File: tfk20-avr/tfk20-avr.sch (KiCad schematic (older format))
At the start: 25 parts, among them J101 USB_C_Receptacle_USB2.0, SW101 SW_Push, U101 ATmega32U4-AU, Y101 16MHz

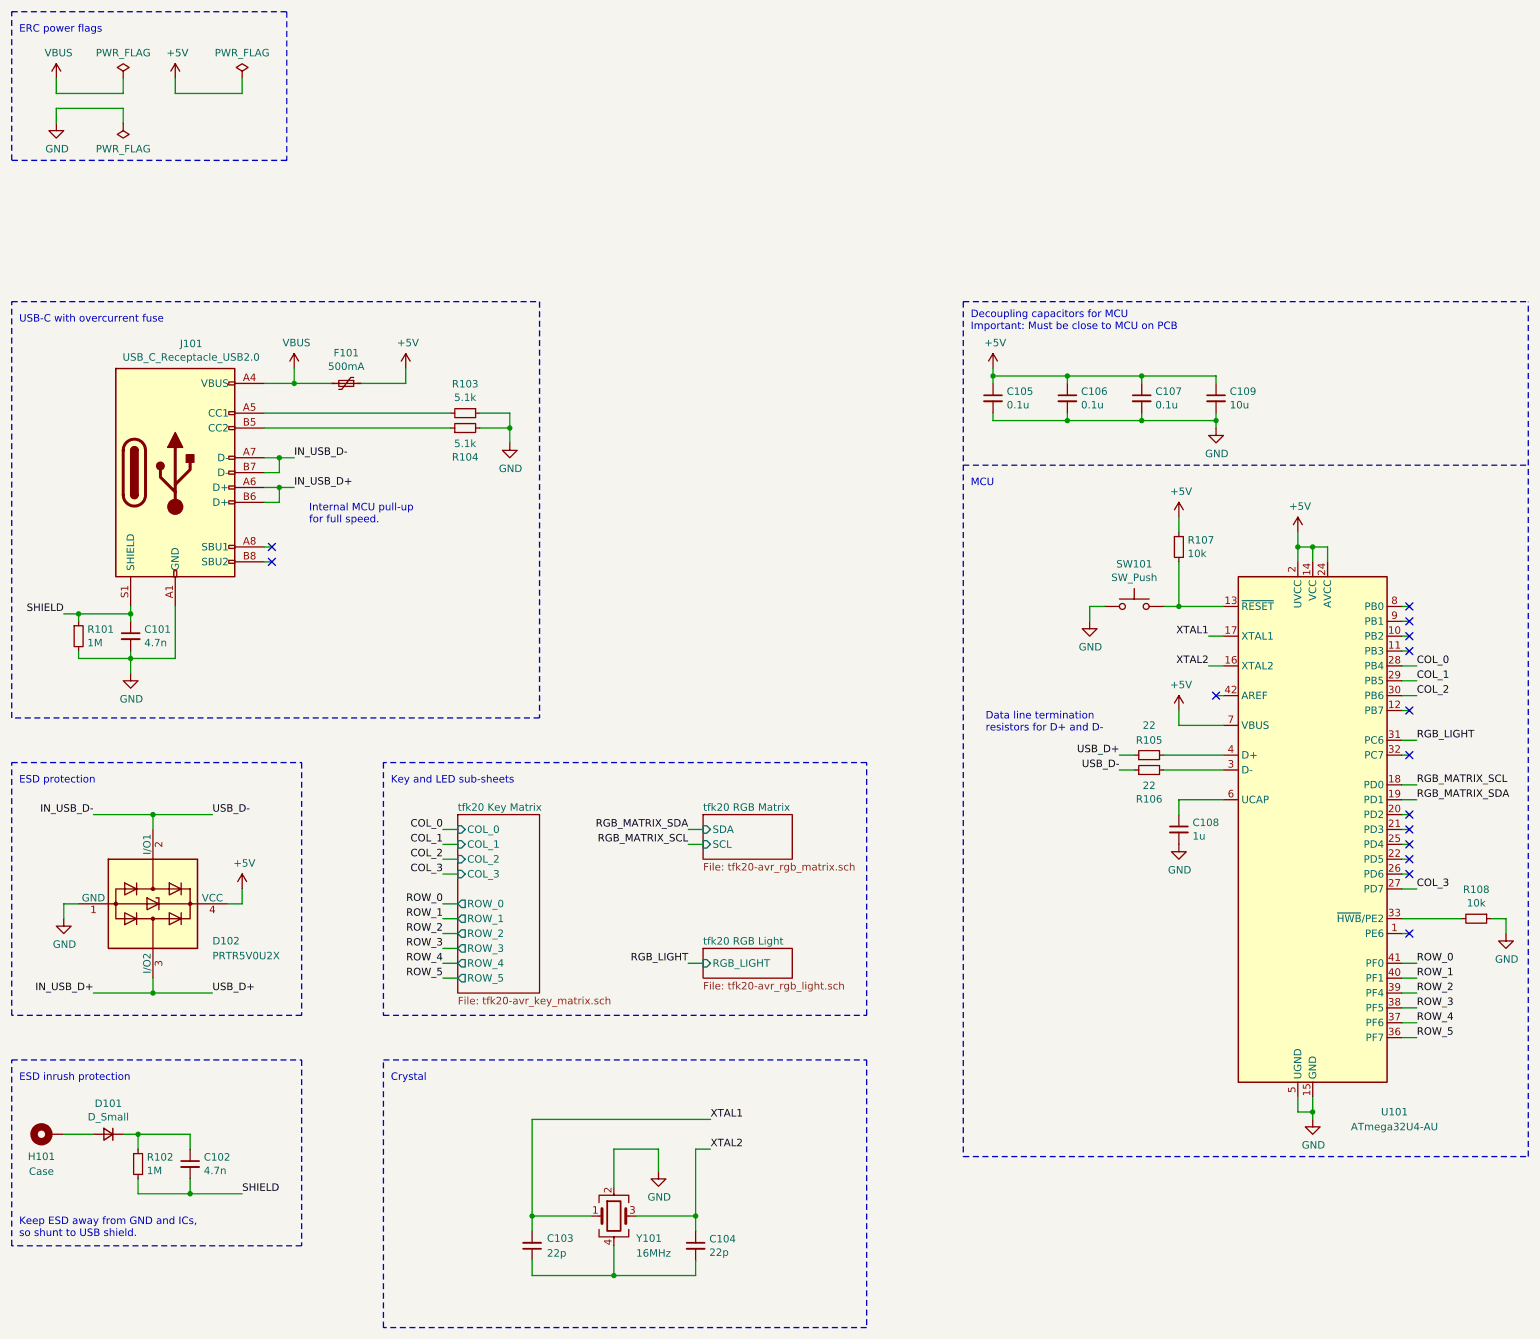
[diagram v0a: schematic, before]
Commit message: Add mounting holes
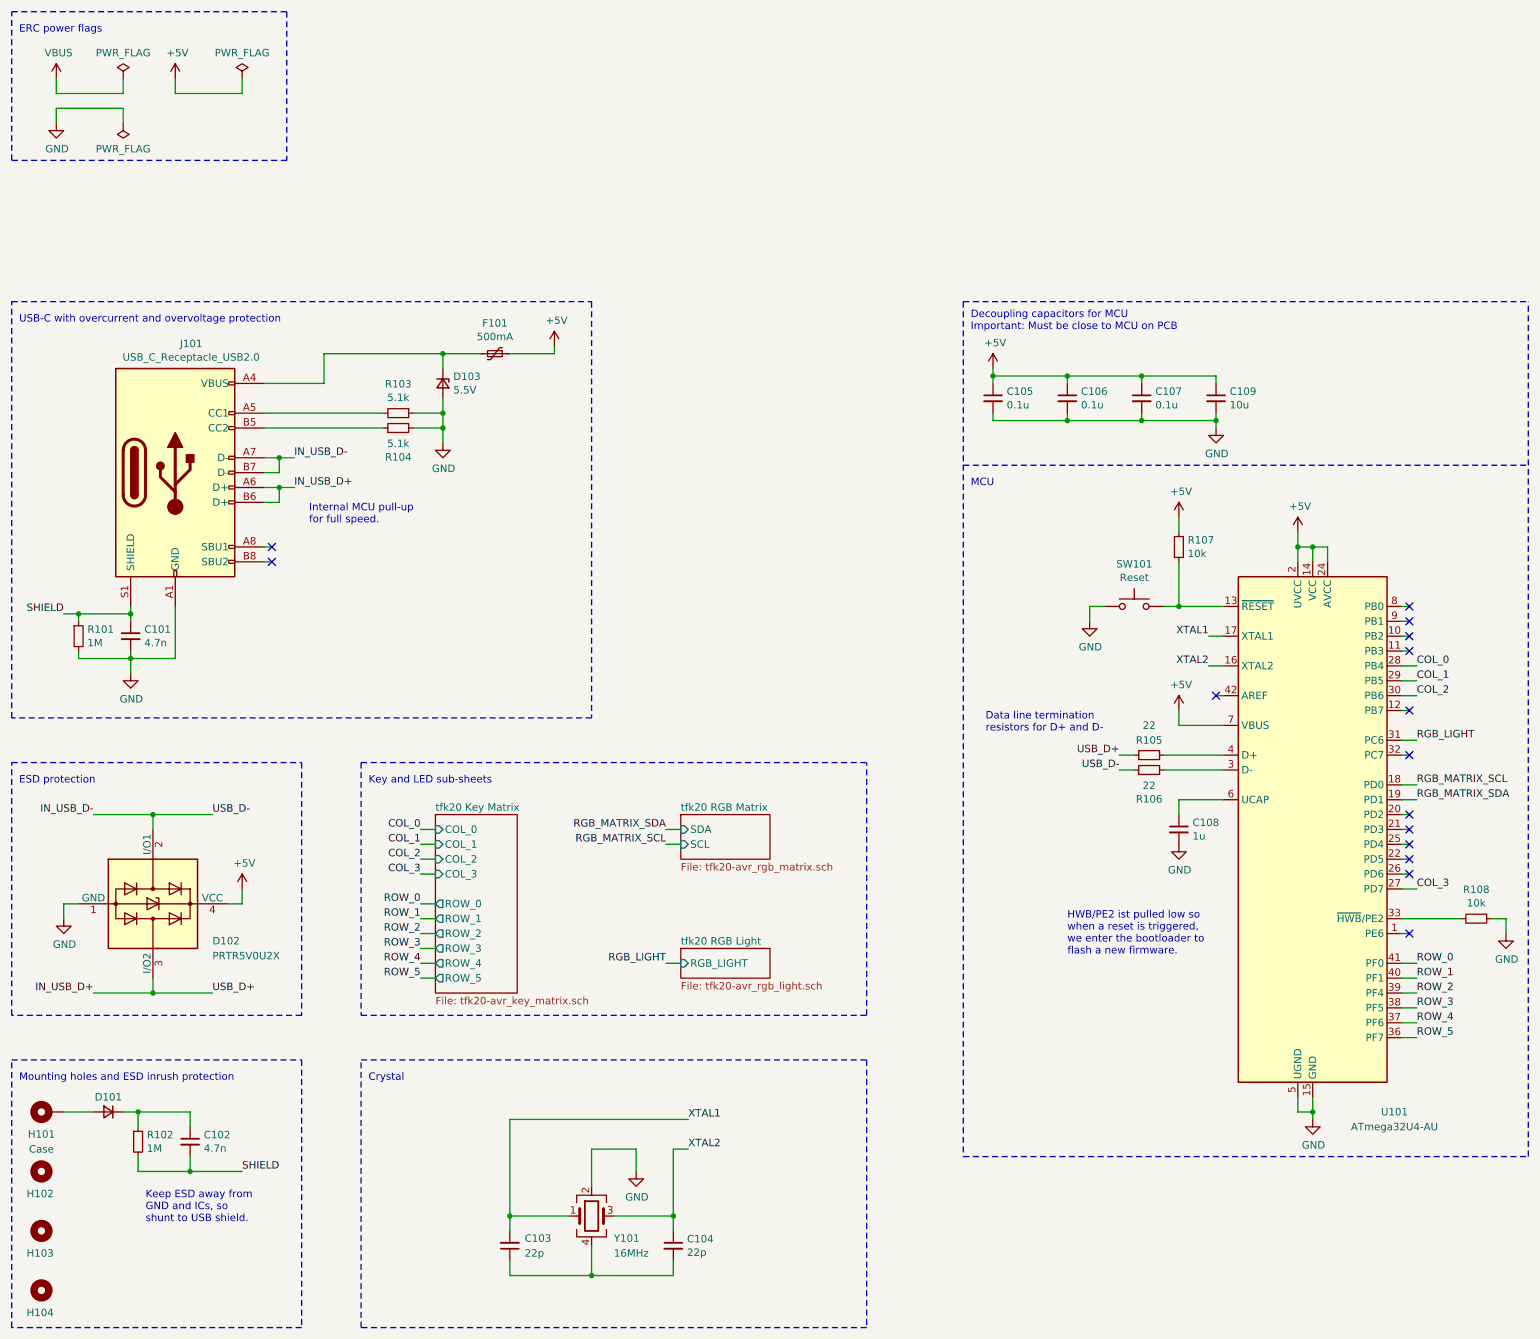
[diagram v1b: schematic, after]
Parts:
- added D103: 5.5V, symbol Device:D_Zener_Small
- added H102, H103, H104: MountingHole, symbol Mechanical:MountingHole
- J101: footprint (none) -> Connector_USB:USB_C_Receptacle_HRO_TYPE-C-31-M-12
- SW101: value SW_Push -> Reset
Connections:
- net GND: now also D103.2 (A)
- net VBUS: no longer F101.2, J101.A4 (VBUS), J101.A9 (VBUS), J101.B4 (VBUS), J101.B9 (VBUS)
- new net: D103.1 (K), F101.2, J101.A4 (VBUS), J101.A9 (VBUS), J101.B4 (VBUS), J101.B9 (VBUS)
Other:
- note added: "HWB/PE2 ist pulled low so\nwhen a reset is triggered,\nwe enter the bootloader to \nflash a new firmware."
- note added: "Keep ESD away from \nGND and ICs, so \nshunt to USB shield."
- note added: "Mounting holes and ESD inrush protection"
- note added: "USB-C with overcurrent and overvoltage protection"
- note removed: "ESD inrush protection"
- note removed: "Keep ESD away from GND and ICs, \nso shunt to USB shield."
- note removed: "USB-C with overcurrent fuse"
- moved on the sheet: C102, C103, C104, D101, F101, H101, R102, R103, R104, Y101

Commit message: Remove alternative switch positions
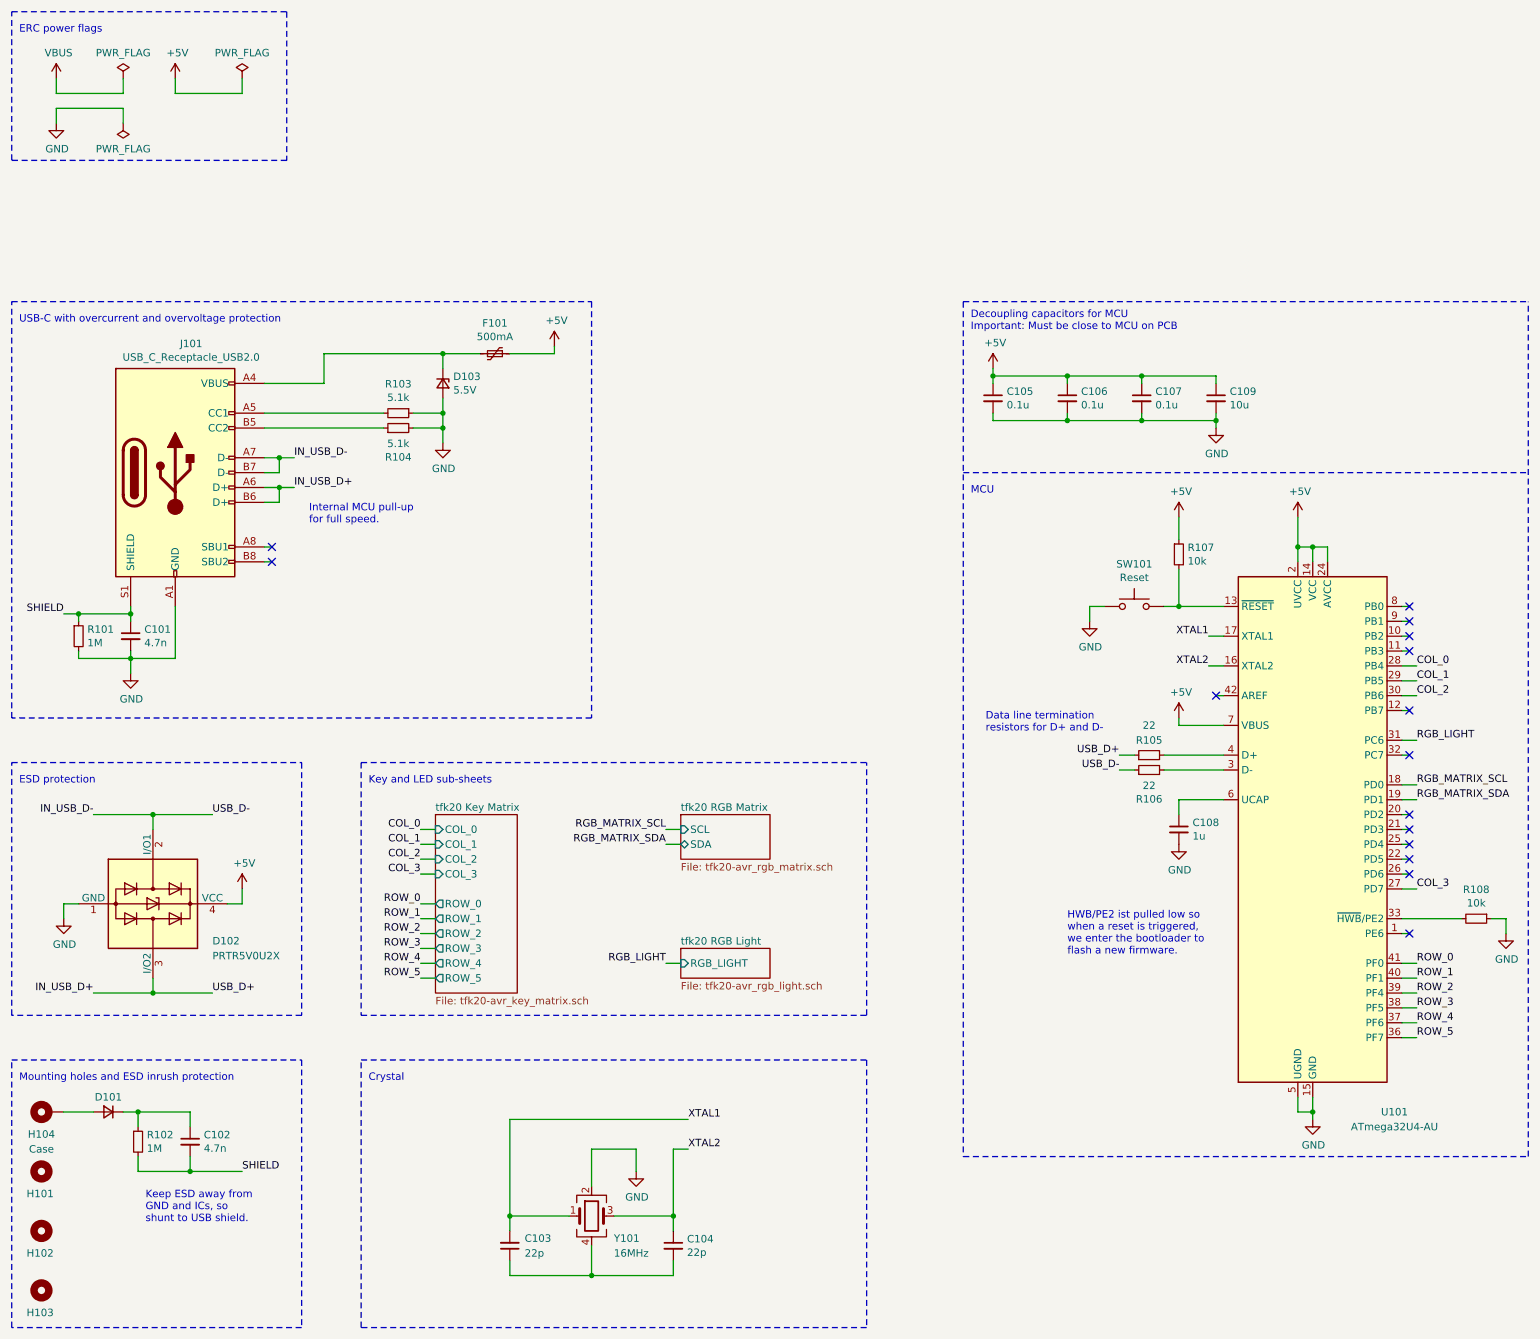
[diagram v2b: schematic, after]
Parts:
- renumbered H102 to H101, H103 to H102, H104 to H103, H101 to H104
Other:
- moved on the sheet: R107
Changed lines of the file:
@@
 F0 "tfk20 RGB Matrix" 50
 F1 "tfk20-avr_rgb_matrix.sch" 50
-F2 "SDA" I L 5200 4250 50
-F3 "SCL" I L 5200 4350 50
+F2 "SDA" B L 5200 4350 50
+F3 "SCL" I L 5200 4250 50
 $EndSheet
 Wire Wire Line
-	5100 4250 5200 4250
-Wire Wire Line
-	5200 4350 5100 4350
+	5100 4350 5200 4350
+Wire Wire Line
+	5200 4250 5100 4250
+Text Label 5100 4350 2    50   ~ 0
+RGB_MATRIX_SDA
 Text Label 5100 4250 2    50   ~ 0
-RGB_MATRIX_SDA
-Text Label 5100 4350 2    50   ~ 0
 RGB_MATRIX_SCL
 Wire Notes Line
@@
 	1250 6150 1050 6150
 $Comp
-L Mechanical:MountingHole_Pad H101
+L Mechanical:MountingHole_Pad H104
 U 1 1 60989184
 P 950 6150
-AR Path="/60989184" Ref="H101"  Part="1"
+AR Path="/60989184" Ref="H104"  Part="1"
 AR Path="/60815FFC/60989184" Ref="H?"  Part="1"
-F 0 "H101" V 800 6200 50  0000 C CNN
+F 0 "H104" V 800 6200 50  0000 C CNN
 F 1 "Case" V 700 6200 50  0000 C CNN
 F 2 "" H 950 6150 50  0001 C CNN
@@
 $EndComp
 $Comp
-L power:+5V #PWR0109
+L power:+5V #PWR0108
 U 1 1 60C2578C
 P 4350 1000
-AR Path="/60C2578C" Ref="#PWR0109"  Part="1"
+AR Path="/60C2578C" Ref="#PWR0108"  Part="1"
 AR Path="/60815FFC/60C2578C" Ref="#PWR?"  Part="1"
-F 0 "#PWR0109" H 4350 850 50  0001 C CNN
+F 0 "#PWR0108" H 4350 850 50  0001 C CNN
 F 1 "+5V" H 4365 1173 50  0000 C CNN
 F 2 "" H 4350 1000 50  0001 C CNN
@@
 Connection ~ 3600 1550
 $Comp
-L power:GND #PWR0108
+L power:GND #PWR0107
 U 1 1 60C257E1
 P 3600 1650
-AR Path="/60C257E1" Ref="#PWR0108"  Part="1"
+AR Path="/60C257E1" Ref="#PWR0107"  Part="1"
 AR Path="/60815FFC/60C257E1" Ref="#PWR?"  Part="1"
-F 0 "#PWR0108" H 3600 1400 50  0001 C CNN
+F 0 "#PWR0107" H 3600 1400 50  0001 C CNN
 F 1 "GND" H 3605 1477 50  0000 C CNN
 F 2 "" H 3600 1650 50  0001 C CNN
@@
 IN_USB_D+
 $Comp
-L power:+5V #PWR0117
+L power:+5V #PWR0116
 U 1 1 60E029DB
-P 9350 2250
-F 0 "#PWR0117" H 9350 2100 50  0001 C CNN
-F 1 "+5V" H 9365 2423 50  0000 C CNN
-F 2 "" H 9350 2250 50  0001 C CNN
-F 3 "" H 9350 2250 50  0001 C CNN
-	1    9350 2250
+P 9350 2150
+F 0 "#PWR0116" H 9350 2000 50  0001 C CNN
+F 1 "+5V" H 9365 2323 50  0000 C CNN
+F 2 "" H 9350 2150 50  0001 C CNN
+F 3 "" H 9350 2150 50  0001 C CNN
+	1    9350 2150
 	1    0    0    -1
 $EndComp
@@
 	9450 2350 9550 2350
 Wire Wire Line
-	9350 2350 9350 2250
+	9350 2350 9350 2150
 Connection ~ 9350 2350
 $Comp
@@
 	10750 4850 10750 4950
 $Comp
-L power:GND #PWR0119
+L power:GND #PWR0118
 U 1 1 60E2D4C6
 P 10750 4950
-F 0 "#PWR0119" H 10750 4700 50  0001 C CNN
+F 0 "#PWR0118" H 10750 4700 50  0001 C CNN
 F 1 "GND" H 10755 4777 50  0000 C CNN
 F 2 "" H 10750 4950 50  0001 C CNN
@@
 	8550 4050 8550 4150
 $Comp
-L power:GND #PWR0115
+L power:GND #PWR0114
 U 1 1 60E7810D
 P 8550 4350
-F 0 "#PWR0115" H 8550 4100 50  0001 C CNN
+F 0 "#PWR0114" H 8550 4100 50  0001 C CNN
 F 1 "GND" H 8555 4177 50  0000 C CNN
 F 2 "" H 8550 4350 50  0001 C CNN
@@
 $EndComp
 $Comp
-L power:+5V #PWR0111
+L power:+5V #PWR0110
 U 1 1 60E7A6BC
 P 7300 1150
-F 0 "#PWR0111" H 7300 1000 50  0001 C CNN
+F 0 "#PWR0110" H 7300 1000 50  0001 C CNN
 F 1 "+5V" H 7315 1323 50  0000 C CNN
 F 2 "" H 7300 1150 50  0001 C CNN
@@
 	7950 2750 7950 2850
 $Comp
-L power:GND #PWR0112
+L power:GND #PWR0111
 U 1 1 60F2F2D5
 P 7950 2850
-F 0 "#PWR0112" H 7950 2600 50  0001 C CNN
+F 0 "#PWR0111" H 7950 2600 50  0001 C CNN
 F 1 "GND" H 7955 2677 50  0000 C CNN
 F 2 "" H 7950 2850 50  0001 C CNN
@@
 L Device:R_Small R107
 U 1 1 60F522E3
-P 8550 2350
-F 0 "R107" H 8609 2396 50  0000 L CNN
-F 1 "10k" H 8609 2305 50  0000 L CNN
-F 2 "" H 8550 2350 50  0001 C CNN
-F 3 "~" H 8550 2350 50  0001 C CNN
-	1    8550 2350
-	1    0    0    -1
-$EndComp
-Wire Wire Line
-	8550 2450 8550 2750
-Wire Wire Line
-	8550 2250 8550 2150
-$Comp
-L power:+5V #PWR0113
+P 8550 2400
+F 0 "R107" H 8609 2446 50  0000 L CNN
+F 1 "10k" H 8609 2355 50  0000 L CNN
+F 2 "" H 8550 2400 50  0001 C CNN
+F 3 "~" H 8550 2400 50  0001 C CNN
+	1    8550 2400
+	1    0    0    -1
+$EndComp
+Wire Wire Line
+	8550 2500 8550 2750
+Wire Wire Line
+	8550 2300 8550 2150
+$Comp
+L power:+5V #PWR0112
 U 1 1 60F64149
 P 8550 2150
-F 0 "#PWR0113" H 8550 2000 50  0001 C CNN
+F 0 "#PWR0112" H 8550 2000 50  0001 C CNN
 F 1 "+5V" H 8565 2323 50  0000 C CNN
 F 2 "" H 8550 2150 50  0001 C CNN
@@
 	8850 3550 8550 3550
 Wire Wire Line
-	8550 3550 8550 3450
-$Comp
-L power:+5V #PWR0114
+	8550 3550 8550 3500
+$Comp
+L power:+5V #PWR0113
 U 1 1 60FA658D
-P 8550 3450
-F 0 "#PWR0114" H 8550 3300 50  0001 C CNN
-F 1 "+5V" H 8565 3623 50  0000 C CNN
-F 2 "" H 8550 3450 50  0001 C CNN
-F 3 "" H 8550 3450 50  0001 C CNN
-	1    8550 3450
+P 8550 3500
+F 0 "#PWR0113" H 8550 3350 50  0001 C CNN
+F 1 "+5V" H 8565 3673 50  0000 C CNN
+F 2 "" H 8550 3500 50  0001 C CNN
+F 3 "" H 8550 3500 50  0001 C CNN
+	1    8550 3500
 	1    0    0    -1
 $EndComp
@@
 Connection ~ 9450 6150
 $Comp
-L power:GND #PWR0118
+L power:GND #PWR0117
 U 1 1 60FDEF5E
 P 9450 6200
-F 0 "#PWR0118" H 9450 5950 50  0001 C CNN
+F 0 "#PWR0117" H 9450 5950 50  0001 C CNN
 F 1 "GND" H 9455 6027 50  0000 C CNN
 F 2 "" H 9450 6200 50  0001 C CNN
@@
 Connection ~ 8800 1500
 $Comp
-L power:GND #PWR0116
+L power:GND #PWR0115
 U 1 1 61059BD9
 P 8800 1550
-AR Path="/61059BD9" Ref="#PWR0116"  Part="1"
+AR Path="/61059BD9" Ref="#PWR0115"  Part="1"
 AR Path="/60815FFC/61059BD9" Ref="#PWR?"  Part="1"
-F 0 "#PWR0116" H 8800 1300 50  0001 C CNN
+F 0 "#PWR0115" H 8800 1300 50  0001 C CNN
 F 1 "GND" H 8805 1377 50  0000 C CNN
 F 2 "" H 8800 1550 50  0001 C CNN
@@
 	1    0    0    -1
 $EndComp
-Text Notes 7150 1950 0    50   ~ 0
+Text Notes 7150 2000 0    50   ~ 0
 MCU
 Wire Notes Line
@@
 	7100 700  7100 6450
 Wire Notes Line
-	7100 1800 10900 1800
+	7100 1850 10900 1850
 Wire Notes Line
 	700  5500 700  3800
@@
 	4900 6550 4900 6400
 $Comp
-L power:GND #PWR0110
+L power:GND #PWR0109
 U 1 1 6122E0FE
 P 4900 6550
-AR Path="/6122E0FE" Ref="#PWR0110"  Part="1"
+AR Path="/6122E0FE" Ref="#PWR0109"  Part="1"
 AR Path="/60815FFC/6122E0FE" Ref="#PWR?"  Part="1"
-F 0 "#PWR0110" H 4900 6300 50  0001 C CNN
+F 0 "#PWR0109" H 4900 6300 50  0001 C CNN
 F 1 "GND" H 4905 6377 50  0000 C CNN
 F 2 "" H 4900 6550 50  0001 C CNN
@@
 	3600 1050 3850 1050
 $Comp
-L Mechanical:MountingHole H102
+L Mechanical:MountingHole H101
 U 1 1 60BC9C45
 P 900 6550
-F 0 "H102" H 800 6400 50  0000 L CNN
+F 0 "H101" H 800 6400 50  0000 L CNN
 F 1 "MountingHole" H 1000 6505 50  0001 L CNN
 F 2 "" H 900 6550 50  0001 C CNN
@@
 $EndComp
 $Comp
-L Mechanical:MountingHole H103
+L Mechanical:MountingHole H102
 U 1 1 60BCA1EE
 P 900 6950
-F 0 "H103" H 800 6800 50  0000 L CNN
+F 0 "H102" H 800 6800 50  0000 L CNN
 F 1 "MountingHole" H 1000 6905 50  0001 L CNN
 F 2 "" H 900 6950 50  0001 C CNN
@@
 $EndComp
 $Comp
-L Mechanical:MountingHole H104
+L Mechanical:MountingHole H103
 U 1 1 60BCA526
 P 900 7350
-F 0 "H104" H 800 7200 50  0000 L CNN
+F 0 "H103" H 800 7200 50  0000 L CNN
 F 1 "MountingHole" H 1000 7305 50  0001 L CNN
 F 2 "" H 900 7350 50  0001 C CNN
